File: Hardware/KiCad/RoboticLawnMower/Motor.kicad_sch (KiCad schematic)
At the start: 11 parts, among them J1 Conn_01x08, Q1 BSS123, Q2 Si7141DP, U1 INA233

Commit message: schaltplan und layout
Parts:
- removed Q1: BSS123, Package_TO_SOT_SMD:SOT-23, symbol Transistor_FET:BSS123
- removed Q2: Si7141DP, Package_SO:PowerPAK_SO-8_Single, symbol Transistor_FET:Si7141DP
- removed R21: 100k, Resistor_SMD:R_0603_1608Metric, symbol Device:R
- removed R6: 100R, Resistor_SMD:R_0603_1608Metric, symbol Device:R
- removed R7: 1M, Resistor_SMD:R_0603_1608Metric, symbol Device:R
- removed R8: 1K, Resistor_SMD:R_0603_1608Metric, symbol Device:R
- added D1: LED_GREEN, LED_SMD:LED_0603_1608Metric, symbol Device:LED
- added R14: 2k2, Resistor_SMD:R_0603_1608Metric, symbol Device:R
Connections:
- net GNDPWR: now also D1.1 (K)
- net MOT_5V_OUT: now also R14.1
- net UBATT: now also R1.2
- net at U1.8 (Vbus): now also R1.4, U1.10 (Vin+); no longer R1.2
- new net: D1.2 (A), R14.2

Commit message: Layout
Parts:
- J1: footprint Connector_JST:JST_XA_B08B-XASK-1-A_1x08_P2.50mm_Vertical -> Connector_JST:JST_XA_B08B-XASK-1_1x08_P2.50mm_Vertical
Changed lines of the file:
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@@
       (effects (font (size 1.27 1.27)) (justify left))
     )
-    (property "Footprint" "Connector_JST:JST_XA_B08B-XASK-1-A_1x08_P2.50mm_Vertical" (id 2) (at 307.34 148.59 0)
+    (property "Footprint" "Connector_JST:JST_XA_B08B-XASK-1_1x08_P2.50mm_Vertical" (id 2) (at 307.34 148.59 0)
       (effects (font (size 1.27 1.27)) hide)
     )

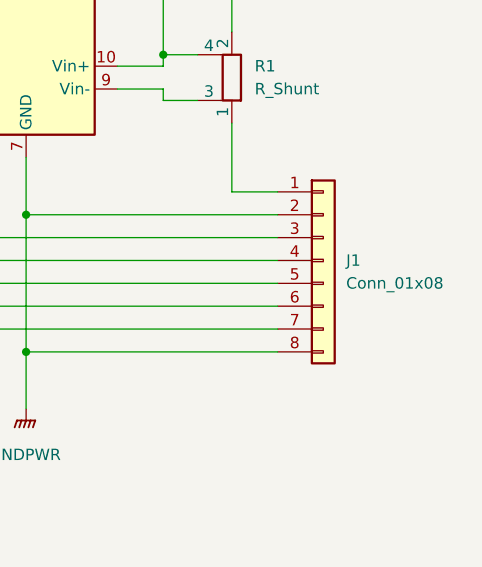
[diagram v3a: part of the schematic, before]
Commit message: Schaltplan & Layout Änderung
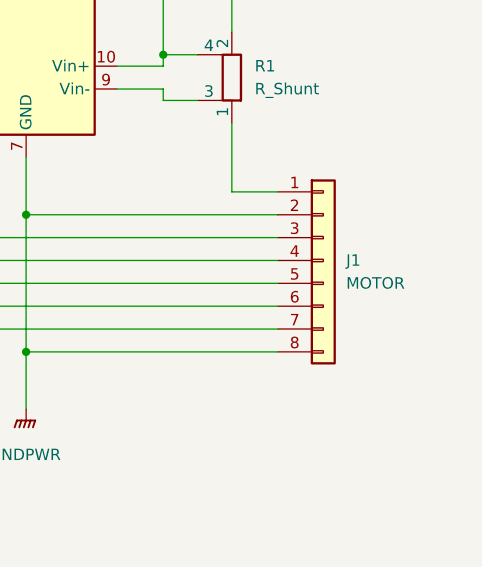
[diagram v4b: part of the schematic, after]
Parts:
- J1: value Conn_01x08 -> MOTOR
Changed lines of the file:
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@@
       (effects (font (size 1.27 1.27)) (justify left))
     )
-    (property "Value" "Conn_01x08" (id 1) (at 309.88 151.1299 0)
+    (property "Value" "MOTOR" (id 1) (at 309.88 151.1299 0)
       (effects (font (size 1.27 1.27)) (justify left))
     )
